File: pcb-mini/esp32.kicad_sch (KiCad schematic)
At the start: 2 parts, among them U9 ESP32-WROOM-E

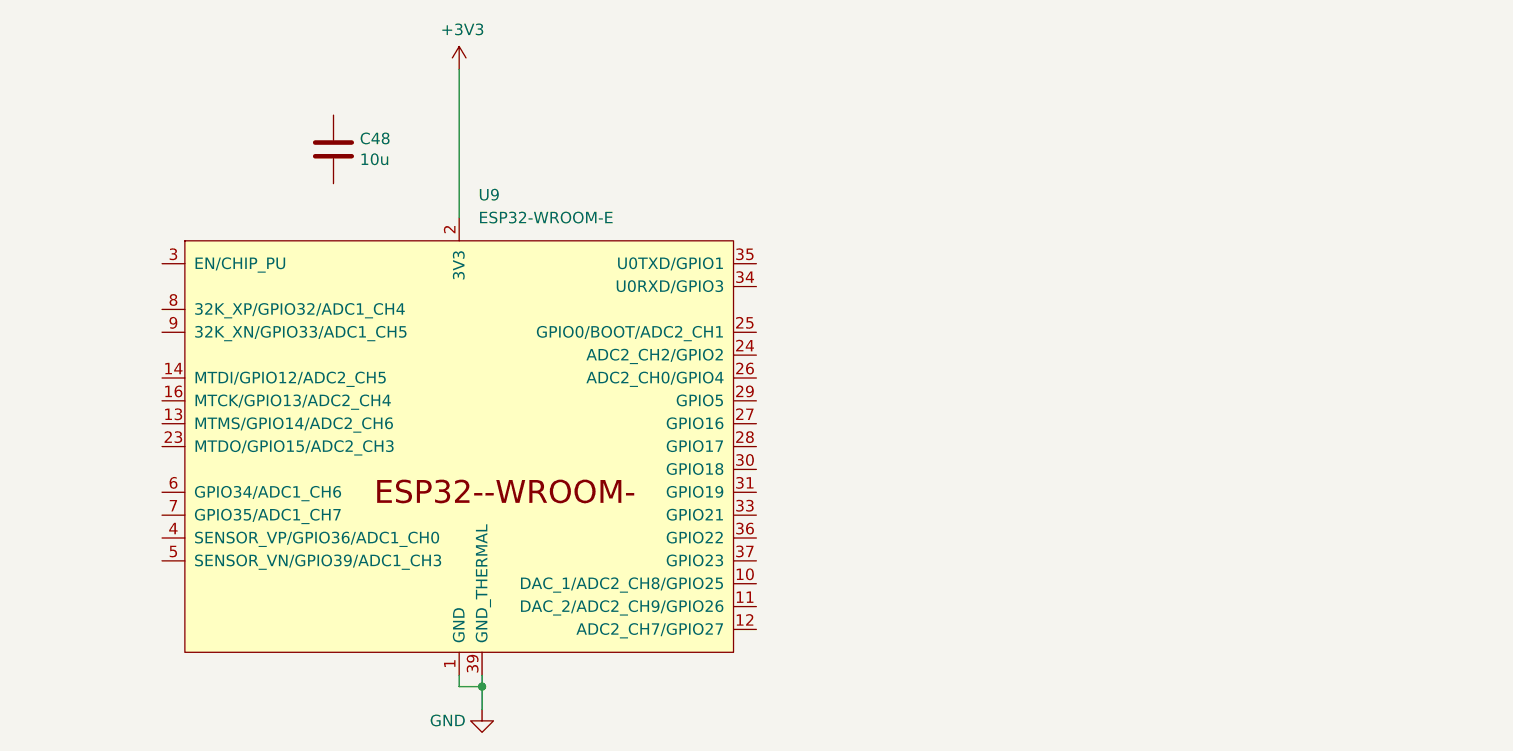
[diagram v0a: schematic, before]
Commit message: [pcb-mini] add ESP32, RM2, route most things
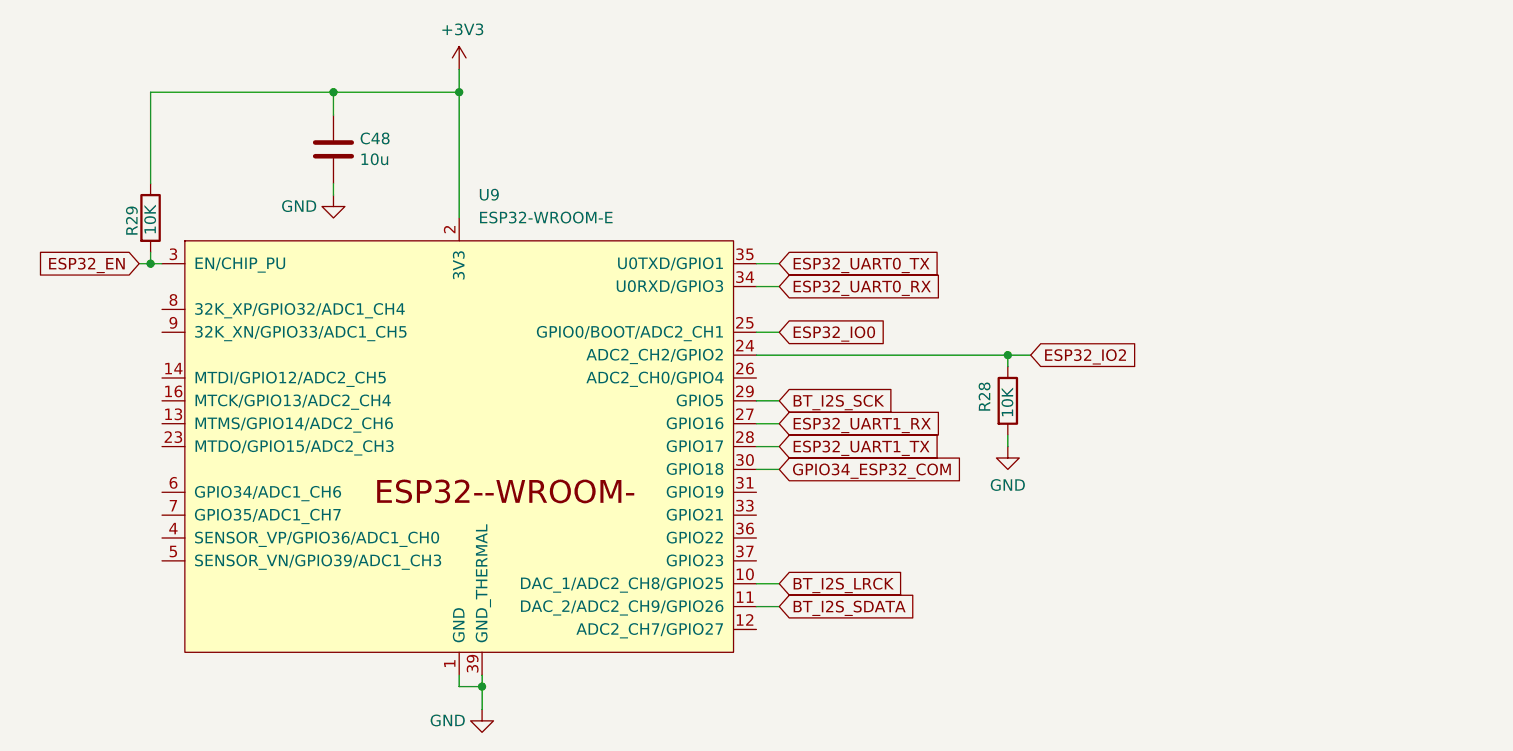
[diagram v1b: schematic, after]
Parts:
- added R28, R29: 10K, Resistor_SMD:R_0603_1608Metric, symbol Device:R
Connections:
- net +3V3: now also C48.1, R29.1
- net GND: now also C48.2, R28.2
- net BT_I2S_LRCK: now reaches U9.10 (DAC_1/ADC2_CH8/GPIO25)
- net BT_I2S_SDATA: now reaches U9.11 (DAC_2/ADC2_CH9/GPIO26)
- net ESP32_IO2: now reaches U9.24 (ADC2_CH2/GPIO2)
- net ESP32_IO2: now also R28.1
- net ESP32_IO0: now reaches U9.25 (GPIO0/BOOT/ADC2_CH1)
- net ESP32_UART1_RX: now reaches U9.27 (GPIO16)
- net ESP32_UART1_TX: now reaches U9.28 (GPIO17)
- net BT_I2S_SCK: now reaches U9.29 (GPIO5)
- net ESP32_EN: now reaches U9.3 (EN/CHIP_PU)
- net ESP32_EN: now also R29.2
- net GPIO34_ESP32_COM: now reaches U9.30 (GPIO18)
- net ESP32_UART0_RX: now reaches U9.34 (U0RXD/GPIO3)
- net ESP32_UART0_TX: now reaches U9.35 (U0TXD/GPIO1)

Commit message: [pcb-mini] fix warnings/errors
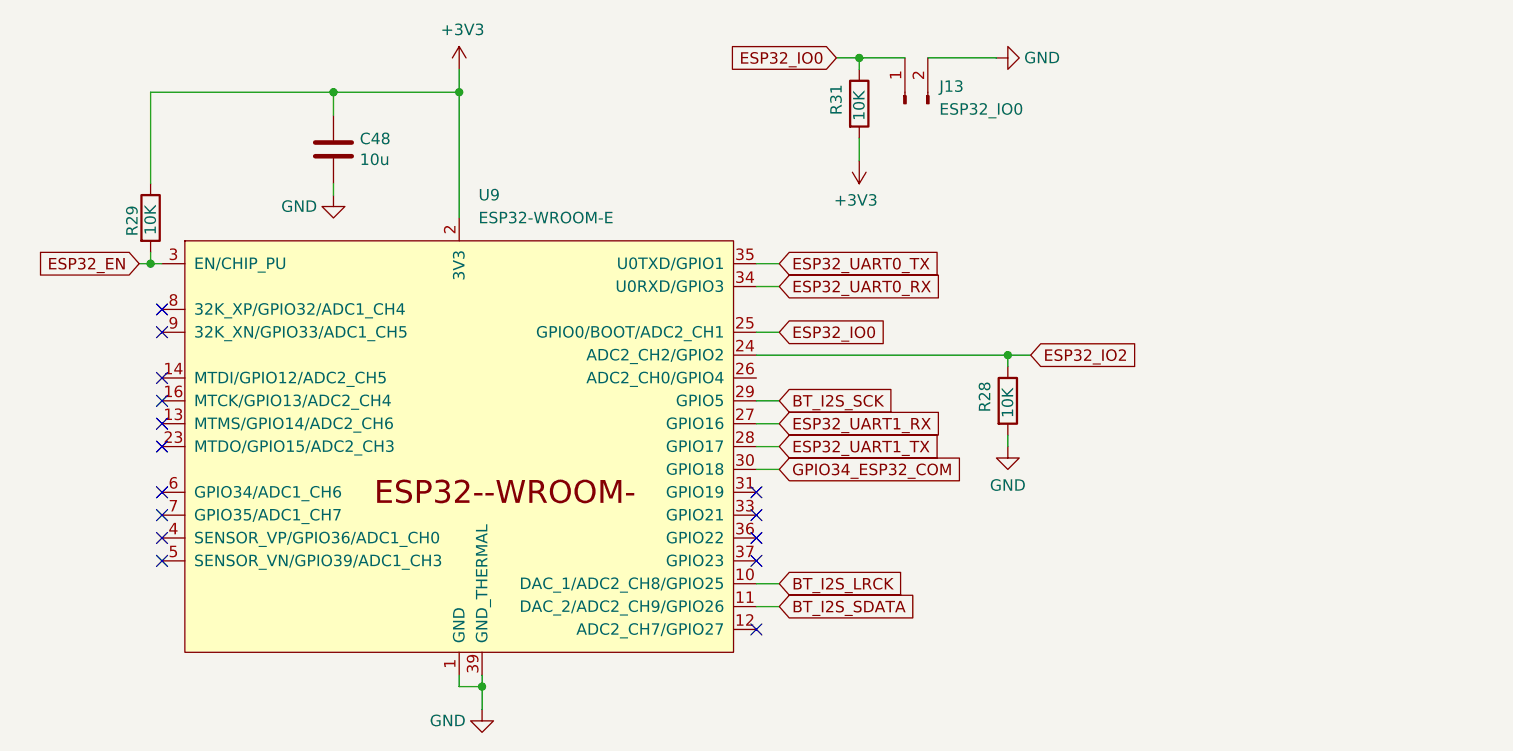
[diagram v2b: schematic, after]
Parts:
- added J13: ESP32_IO0, Connector_PinHeader_2.54mm:PinHeader_1x02_P2.54mm_Vertical, symbol Connector:Conn_01x02_Pin
- added R31: 10K, Resistor_SMD:R_0603_1608Metric, symbol Device:R
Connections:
- net +3V3: now also R31.2
- net ESP32_IO0: now also J13.1 (Pin_1), R31.1
- net GND: now also J13.2 (Pin_2)
- no-connect marks 0 -> 15

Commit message: [pcb] mini: add/fix LCSC refs
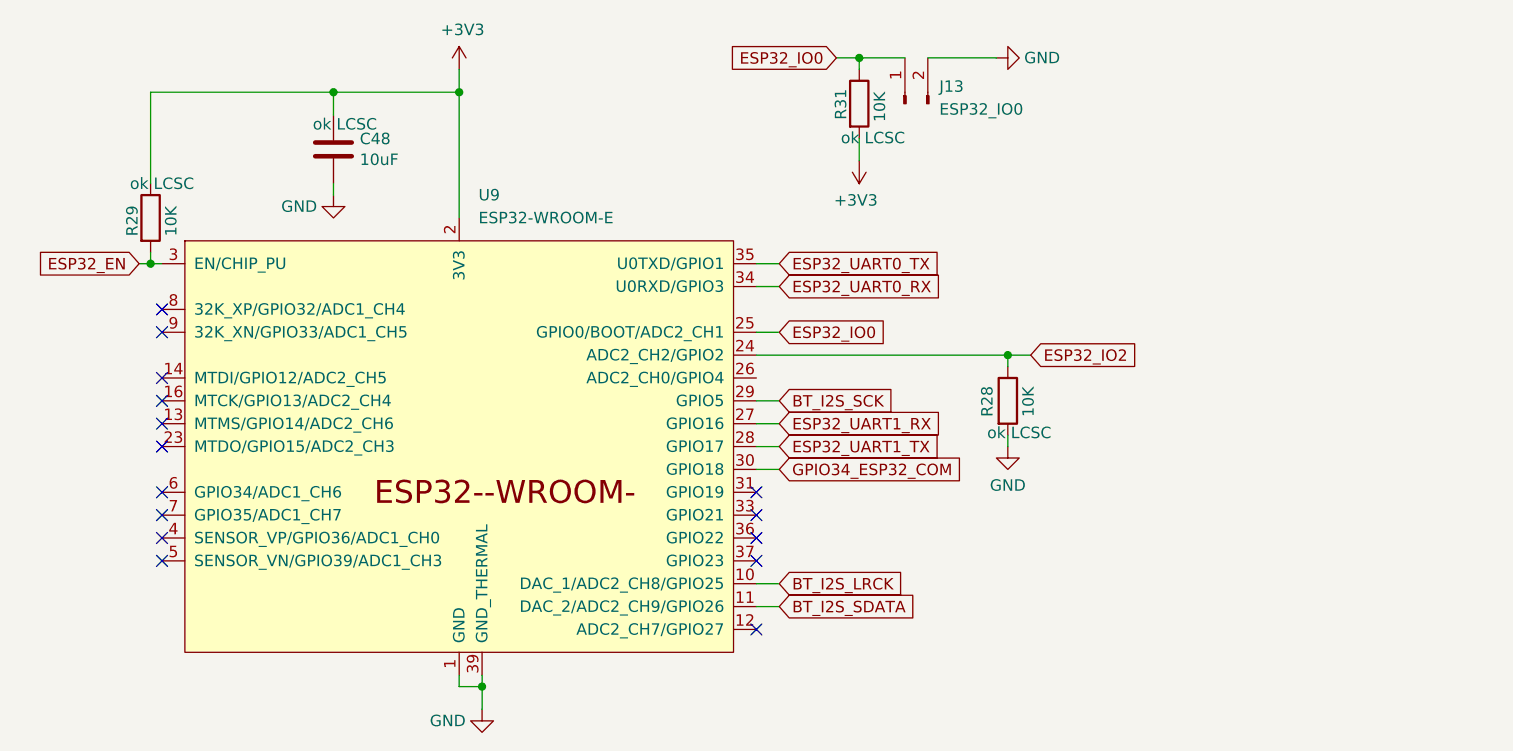
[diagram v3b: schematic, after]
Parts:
- C48: value 10u -> 10uF; LCSC (none) -> C15850
- R28, R29, R31: footprint Resistor_SMD:R_0603_1608Metric -> Resistor_SMD:R_0402_1005Metric
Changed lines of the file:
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@@
 			)
 		)
-		(property "Value" "10u"
+		(property "Value" "10uF"
 			(at 114.681 55.753 0)
 			(effects
@@
 			)
 		)
-		(property "Description" ""
+		(property "Description" "ok LCSC"
+			(at 113.03 51.816 0)
+			(effects
+				(font
+					(size 1.27 1.27)
+				)
+			)
+		)
+		(property "LCSC" "C15850"
 			(at 111.76 54.61 0)
 			(effects
@@
 					(size 1.27 1.27)
 				)
+				(hide yes)
 			)
 		)
@@
 		(dnp no)
 		(property "Reference" "R28"
-			(at 184.15 83.82 90)
+			(at 184.404 84.328 90)
 			(effects
 				(font
@@
 		)
 		(property "Value" "10K"
-			(at 186.69 84.455 90)
-			(effects
-				(font
-					(size 1.27 1.27)
-				)
-				(justify left)
-			)
-		)
-		(property "Footprint" "Resistor_SMD:R_0603_1608Metric"
+			(at 188.976 84.328 90)
+			(effects
+				(font
+					(size 1.27 1.27)
+				)
+				(justify left)
+			)
+		)
+		(property "Footprint" "Resistor_SMD:R_0402_1005Metric"
 			(at 184.912 82.55 90)
 			(effects
@@
 			)
 		)
-		(property "Description" ""
-			(at 186.69 82.55 0)
-			(effects
-				(font
-					(size 1.27 1.27)
-				)
-				(hide yes)
+		(property "Description" "ok LCSC"
+			(at 187.96 86.106 0)
+			(effects
+				(font
+					(size 1.27 1.27)
+				)
 			)
 		)
@@
 		)
 		(property "Value" "10K"
-			(at 91.44 64.135 90)
-			(effects
-				(font
-					(size 1.27 1.27)
-				)
-				(justify left)
-			)
-		)
-		(property "Footprint" "Resistor_SMD:R_0603_1608Metric"
+			(at 93.726 64.262 90)
+			(effects
+				(font
+					(size 1.27 1.27)
+				)
+				(justify left)
+			)
+		)
+		(property "Footprint" "Resistor_SMD:R_0402_1005Metric"
 			(at 89.662 62.23 90)
 			(effects
@@
 			)
 		)
-		(property "Description" ""
-			(at 91.44 62.23 0)
-			(effects
-				(font
-					(size 1.27 1.27)
-				)
-				(hide yes)
+		(property "Description" "ok LCSC"
+			(at 92.71 58.42 0)
+			(effects
+				(font
+					(size 1.27 1.27)
+				)
 			)
 		)
@@
 		(dnp no)
 		(property "Reference" "R31"
-			(at 167.64 50.8 90)
+			(at 168.148 51.308 90)
 			(effects
 				(font
@@
 		)
 		(property "Value" "10K"
-			(at 170.18 51.435 90)
-			(effects
-				(font
-					(size 1.27 1.27)
-				)
-				(justify left)
-			)
-		)
-		(property "Footprint" "Resistor_SMD:R_0603_1608Metric"
+			(at 172.466 51.562 90)
+			(effects
+				(font
+					(size 1.27 1.27)
+				)
+				(justify left)
+			)
+		)
+		(property "Footprint" "Resistor_SMD:R_0402_1005Metric"
 			(at 168.402 49.53 90)
 			(effects
@@
 			)
 		)
-		(property "Description" ""
-			(at 170.18 49.53 0)
-			(effects
-				(font
-					(size 1.27 1.27)
-				)
-				(hide yes)
-			)
-		)
+		(property "Description" "ok LCSC"
+			(at 171.704 53.34 0)
+			(effects
+				(font
+					(size 1.27 1.27)
+				)
+			)
+		)

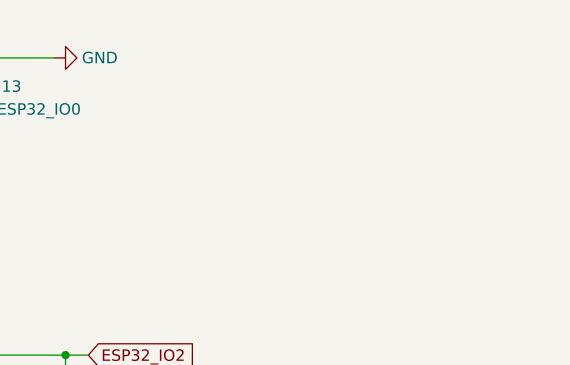
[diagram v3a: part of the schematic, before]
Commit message: [pcb] mini: move boot btn, add silkscreen, add con for ESP32 UART
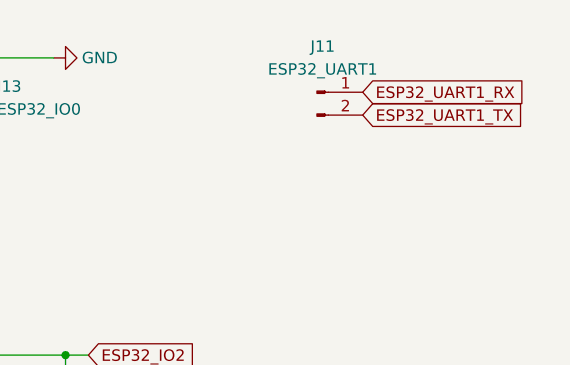
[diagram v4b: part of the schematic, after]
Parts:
- added J11: ESP32_UART1, Connector_PinHeader_2.54mm:PinHeader_1x02_P2.54mm_Vertical, symbol Connector:Conn_01x02_Pin
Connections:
- net ESP32_UART1_RX: now also J11.1 (Pin_1)
- net ESP32_UART1_TX: now also J11.2 (Pin_2)
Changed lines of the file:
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@@
+		)
+	)
+	(global_label "ESP32_UART1_RX"
+		(shape input)
+		(at 219.71 48.26 0)
+		(fields_autoplaced yes)
+		(effects
+			(font
+				(size 1.27 1.27)
+			)
+			(justify left)
+		)
+		(property "Intersheetrefs" "${INTERSHEET_REFS}"
+			(at 239.0236 48.26 0)
+			(effects
+				(font
+					(size 1.27 1.27)
+				)
+				(justify left)
+				(hide yes)
+			)
 		)
 	)
@@
 		)
 	)
+	(global_label "ESP32_UART1_TX"
+		(shape input)
+		(at 219.71 50.8 0)
+		(fields_autoplaced yes)
+		(effects
+			(font
+				(size 1.27 1.27)
+			)
+			(justify left)
+		)
+		(property "Intersheetrefs" "${INTERSHEET_REFS}"
+			(at 238.7212 50.8 0)
+			(effects
+				(font
+					(size 1.27 1.27)
+				)
+				(justify left)
+				(hide yes)
+			)
+		)
+	)
 	(global_label "ESP32_IO0"
 		(shape input)
@@
 					(unit 1)
 				)
+			)
+		)
+	)
+	(symbol
+		(lib_id "Connector:Conn_01x02_Pin")
+		(at 214.63 48.26 0)
+		(unit 1)
+		(exclude_from_sim no)
+		(in_bom yes)
+		(on_board yes)
+		(dnp no)
+		(fields_autoplaced yes)
+		(property "Reference" "J11"
+			(at 215.265 43.18 0)
+			(effects
+				(font
+					(size 1.27 1.27)
+				)
+			)
+		)
+		(property "Value" "ESP32_UART1"
+			(at 215.265 45.72 0)
+			(effects
+				(font
+					(size 1.27 1.27)
+				)
+			)
+		)
+		(property "Footprint" "Connector_PinHeader_2.54mm:PinHeader_1x02_P2.54mm_Vertical"
+			(at 214.63 48.26 0)
+			(effects
+				(font
+					(size 1.27 1.27)
+				)
+				(hide yes)
+			)
+		)
+		(property "Datasheet" "~"
+			(at 214.63 48.26 0)
+			(effects
+				(font
+					(size 1.27 1.27)
+				)
+				(hide yes)
+			)
+		)
+		(property "Description" "Generic connector, single row, 01x02, script generated"
+			(at 214.63 48.26 0)
+			(effects
+				(font
+					(size 1.27 1.27)
+				)
+				(hide yes)
+			)
+		)
+		(pin "1"
+		)
+		(pin "2"
+		)
+		(instances
+			(project "picoclock"
+				(path "/3b9dec0e-e0b7-4565-afc9-c4692f41aea9/1300d4ba-b6e1-492a-b576-039297edc301"
+					(reference "J11")
+					(unit 1)
+				)
